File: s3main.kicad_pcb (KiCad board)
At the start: 2 copper layers, 75 x 60 mm, 147 parts, among them J1 TRACK, J2 IDC, J3 POWER, J4 USB_C_Receptacle_USB2.0_16P, J5 ZUSI, Q1 QS6K21, Q10 BC847B, Q11 BC847B, Q2 BC847BDW1, Q3 SiS4634LDN, Q4 SiS4634LDN, Q5 SiS4634LDN, Q6 QS6K21, Q7 SiS4634LDN, Q8 SiS4634LDN, Q9 BC857B, SW1 EN, SW2 BOOT, U1 LM393, U10 BTS4141N, U2 7402, U3 TLV9061xDBV, U4 ESP32-S3-WROOM-2, U5 DRV8328B, U6 TPS281C100A, U7 AP63205WU, U8 TXS0102DCT, U9 AZ1117-3.3

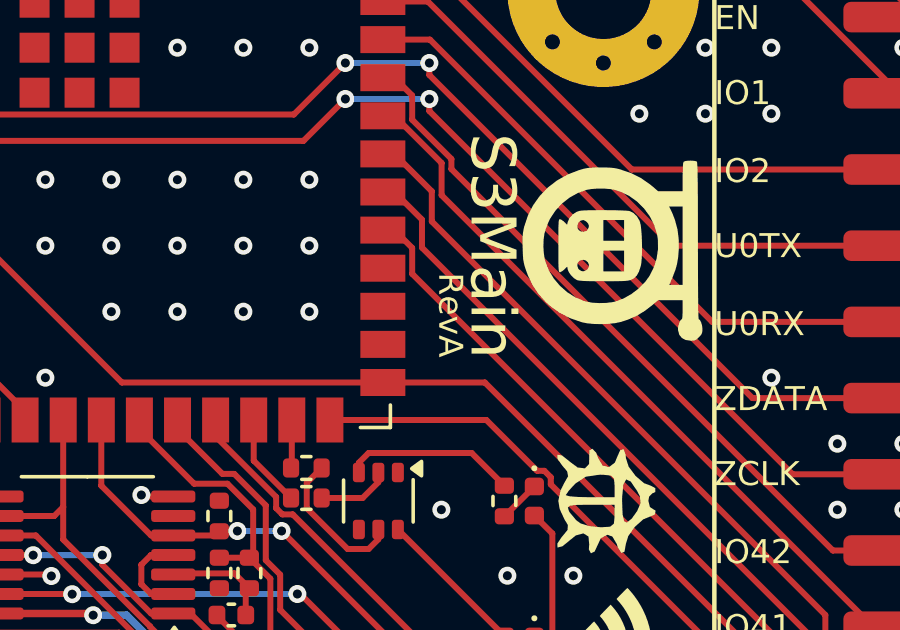
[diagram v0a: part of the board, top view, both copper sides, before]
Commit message: chore: switch to semantic versioning
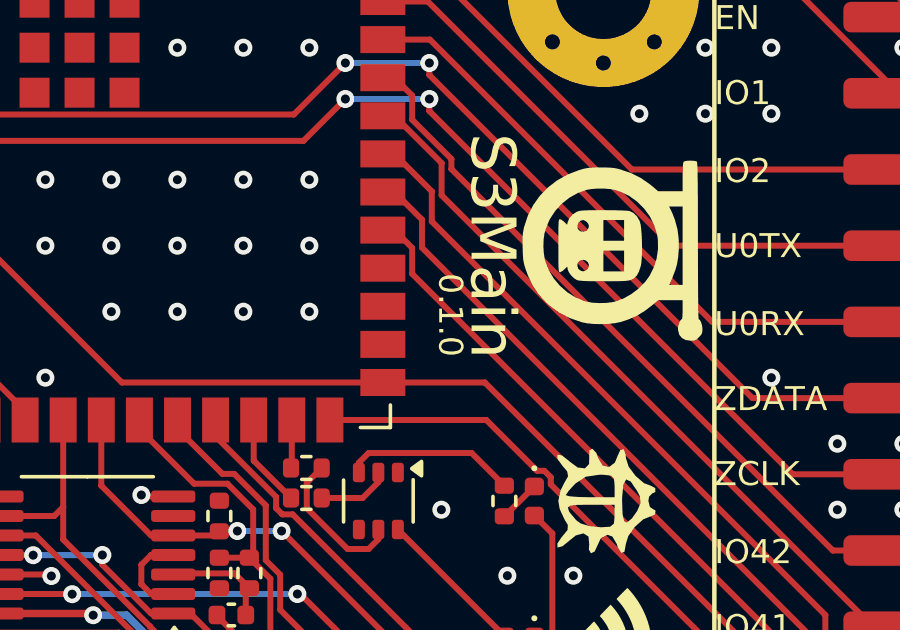
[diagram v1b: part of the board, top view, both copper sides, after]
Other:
- board text added: "0.1.0"
- board text removed: "RevA"
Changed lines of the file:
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@@
 		)
 	)
-	(gr_text "RevA"
+	(gr_text "0.1.0"
 		(at 164.1 83.3 270)
 		(layer "F.SilkS")

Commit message: feat: new ACK circuit
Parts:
- removed the Q10 at (136.4, 100.6)
- removed the R50 at (137.5, 108.2)
- removed the R52 at (137.4, 103.0)
- added C31: 10n, Capacitor_SMD:C_1206_3216Metric, F.Cu at (137.6, 105.4)
- added D14: B5819W, Diode_SMD:D_SOD-123, F.Cu at (134.5, 99.4)
- added D15: B5819W, Diode_SMD:D_SOD-123, F.Cu at (135.3, 105.4)
- added D18: SBR3U60P1, Diode_SMD:D_PowerDI-123, F.Cu at (125.0, 114.8)
- added R54: 10k, Resistor_SMD:R_0402_1005Metric, F.Cu at (139.6, 97.7)
- Q9: value BC857B -> BSS138; footprint Package_TO_SOT_SMD:SOT-23-3 -> Package_TO_SOT_SMD:TSOT-23
- R49: value 1k -> 4k7
- R51: value 22k -> 1k
- moved Q9 6.68 mm to (137.4, 99.0)
- moved R50 4.03 mm to (136.2, 102.1), turned to -90 degrees
- moved R49 3.83 mm to (137.4, 108.2), turned to 180 degrees
- moved R51 2.01 mm to (137.2, 102.1), turned to 90 degrees
- renumbered C31 to C32, C32 to C33, C33 to C34, C34 to C35, C35 to C36, C36 to C37, D14 to D16, D15 to D17, D17 to D19, Q11 to Q10, R55 to R50, R53 to R52, R54 to R53, R56 to R55
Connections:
- J5 pad 4: Net-(J5-Pin_4) -> Net-(D18-K)
- Q9 pad 1: Net-(Q9-B) -> Net-(Q9-G)
- Q9 pad 2: VDC -> GND
- Q9 pad 3: Net-(Q9-C) -> ACK
- R49 pad 1: VDC -> Vdrive
- R49 pad 2: Net-(Q9-B) -> Net-(C31-Pad1)
- R50 pad 1: +3V3 -> +5V
- R50 pad 2: ACK -> Net-(D14-A)
- R51 pad 1: Net-(Q9-C) -> Net-(D14-A)
- R51 pad 2: Net-(Q10-B) -> Net-(Q9-G)
- U10 pad 1: Net-(J5-Pin_4) -> Net-(D18-A)
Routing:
- net +5V: track 214.3 -> 236.5 mm, vias 6 -> 7
- net Net-(D18-K): track 0.00 -> 11.7 mm
- net Net-(J5-Pin_4): track 8.59 -> 0.00 mm
- net Net-(D14-A): track 0.00 -> 6.54 mm
- net +3V3: track 297.7 -> 303.5 mm
- net Net-(Q9-B): track 3.45 -> 0.00 mm
- net Net-(Q10-B): track 2.63 -> 0.00 mm
- net Net-(D18-A): track 0.00 -> 2.22 mm
- net Net-(Q9-C): track 2.12 -> 0.00 mm
- net Net-(C31-Pad1): track 0.00 -> 1.62 mm
- net Net-(Q9-G): track 0.00 -> 1.59 mm
- net ACK: track 21.8 -> 20.4 mm
- net VDC: track 174.5 -> 173.7 mm
- net GND: vias 237 -> 231
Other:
- board text added: "10-22V="
- board text removed: "10-27V="
